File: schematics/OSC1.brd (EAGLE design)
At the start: 23.2 x 49.5 mm, 23 parts

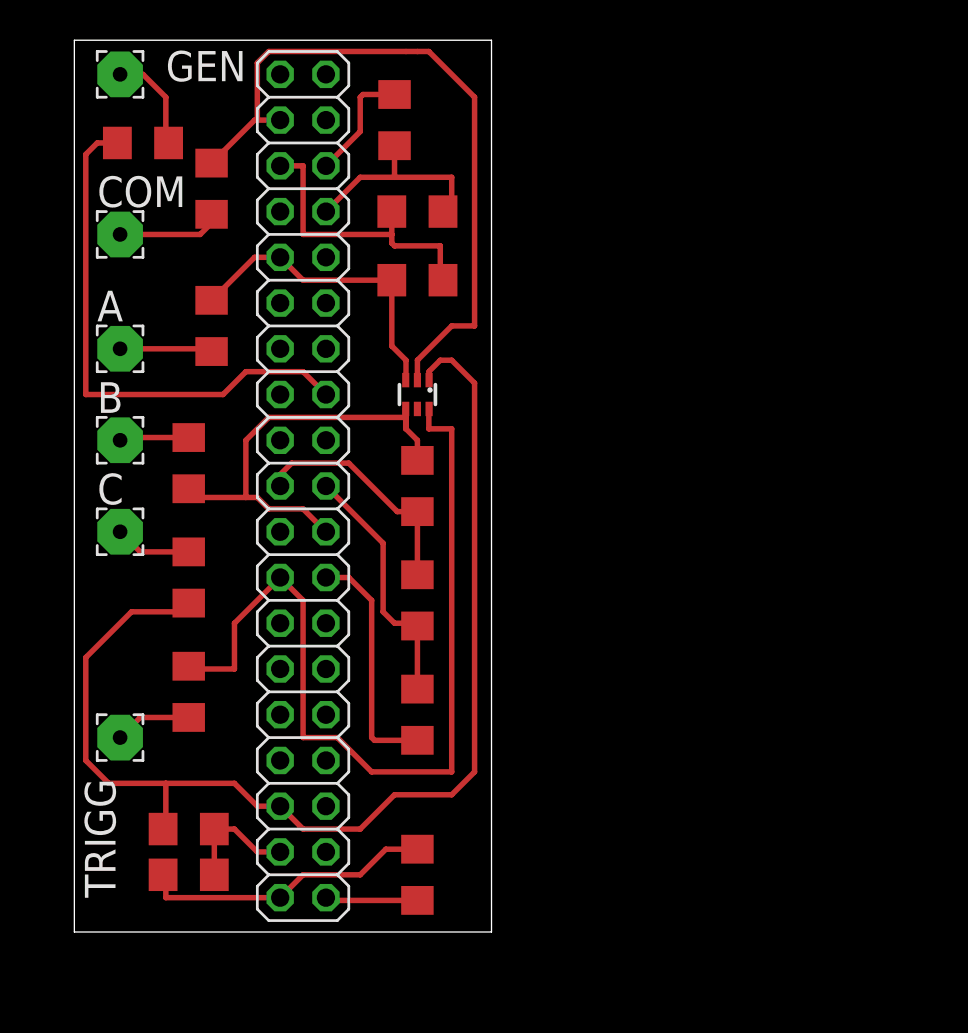
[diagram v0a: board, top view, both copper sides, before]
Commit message: - Electrical parameters change - schematics + readme
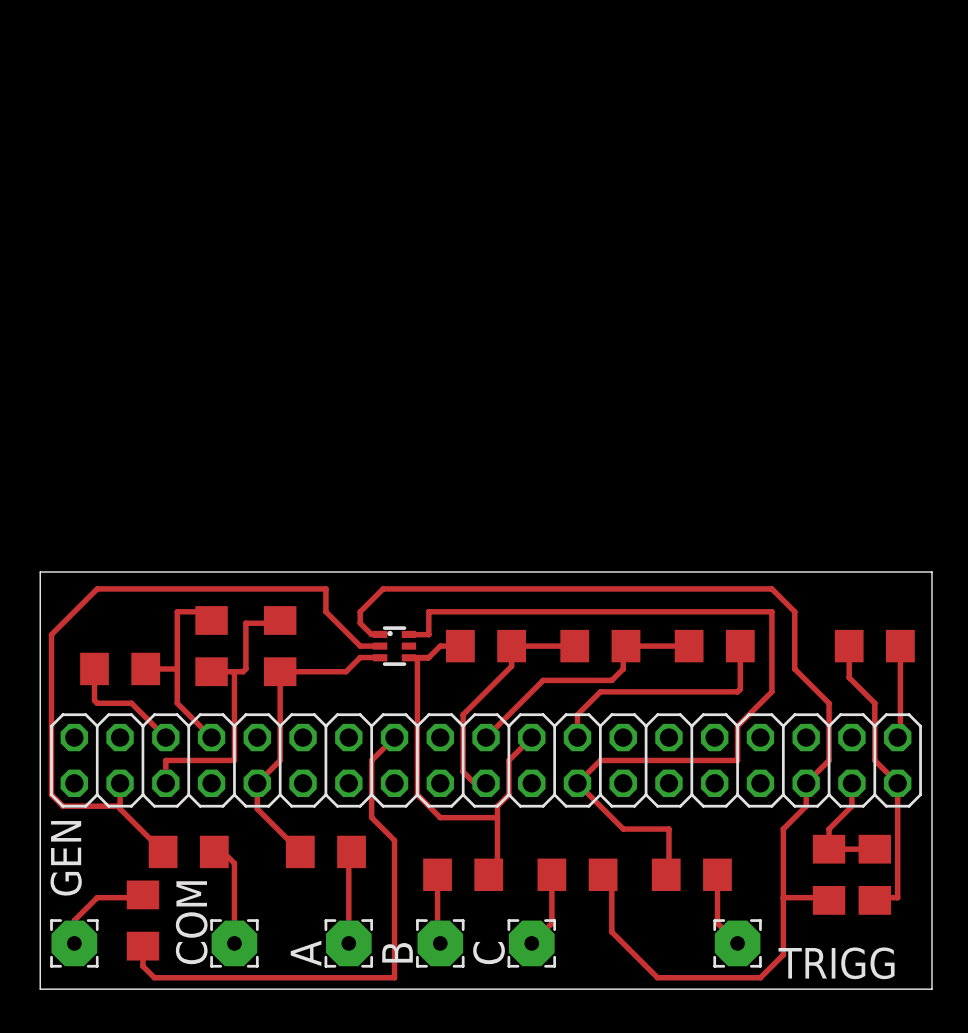
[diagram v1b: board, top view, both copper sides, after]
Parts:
- R1, R2, R3: value 910K -> 30K
- R10, R13, R16: value 68K -> N/A
- R11, R14, R17: value 820K -> N/A
- R12, R15, R9: value 30K -> 3.3K
- R18: value 20K -> 3.3K
- moved GEN 48.3 mm to (1.91, 3.17), turned to 90 degrees
- moved R18 43.2 mm to (5.71, 4.45), turned to 270 degrees
- moved COM 39.9 mm to (10.8, 3.17), turned to 90 degrees
- moved R10 38.1 mm to (46.4, 6.99), turned to 270 degrees
- moved R5 36.9 mm to (8.26, 8.26), turned to 180 degrees
- moved TRIGG 36.1 mm to (38.7, 3.17), turned to 90 degrees
- moved R9 35.7 mm to (43.8, 6.99), turned to 90 degrees
- moved A 35.4 mm to (17.1, 3.17), turned to 90 degrees
- moved R17 34.1 mm to (4.45, 18.4), turned to 180 degrees
- moved B 33.1 mm to (22.2, 3.17), turned to 90 degrees
- moved C 32.3 mm to (27.3, 3.17), turned to 90 degrees
- moved R1 29.9 mm to (15.9, 8.26), turned to 180 degrees
- moved R4 29.7 mm to (36.2, 6.99), turned to 180 degrees
- moved R11 28.4 mm to (46.4, 19.7), turned to 0 degrees
- moved R2 27.5 mm to (23.5, 6.99), turned to 0 degrees
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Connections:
- net A2 renamed BAD_A2
- net B2 renamed BAD_B2
- net C2 renamed BAD_C2
- removed net A30: JP1.5, R15.2, R16.1
- removed net B30: JP1.19, R12.2, R13.1
- removed net C30: JP1.35, R10.1, R9.2
- new net BAD_A10: JP1.8, R16.2, R17.1
- new net BAD_B10: JP1.20, R13.2, R14.1
- new net BAD_C10: JP1.37, R10.2, R11.1
- net A10: now also JP1.5, R15.2, R16.1; no longer JP1.8, R16.2, R17.1
- net B10: now also JP1.19, R12.2, R13.1; no longer JP1.20, R13.2, R14.1
- net C10: now also JP1.35, R10.1, R9.2; no longer JP1.37, R10.2, R11.1
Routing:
- net A30: track 16.5 -> 0.00 mm
- net BAD_C10: track 0.00 -> 16.4 mm
- net BAD_B10: track 0.00 -> 14.0 mm
- net B30: track 13.1 -> 0.00 mm
- net BAD_A10: track 0.00 -> 11.6 mm
- net C10: track 16.4 -> 6.72 mm
- net C30: track 6.72 -> 0.00 mm
- net A10: track 11.6 -> 16.5 mm
- net B10: track 14.0 -> 13.1 mm
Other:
- board size 23.2 x 49.5 mm -> 49.5 x 23.2 mm
